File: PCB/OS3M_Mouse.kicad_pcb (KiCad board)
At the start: 4 copper layers, 60.8 x 61.3 mm, 47 parts, among them J1 DBG_HDR, J2 USB_C_Receptacle_USB2.0, J3 EXP_HDR, SW1 SW_Push, U1 AP2112K-3.3, U2 LDC1614, U3 STM32F042F6P6, U4 LDC1612, U5 USBLC6-2SC6, X1 ASV-40.000MHz

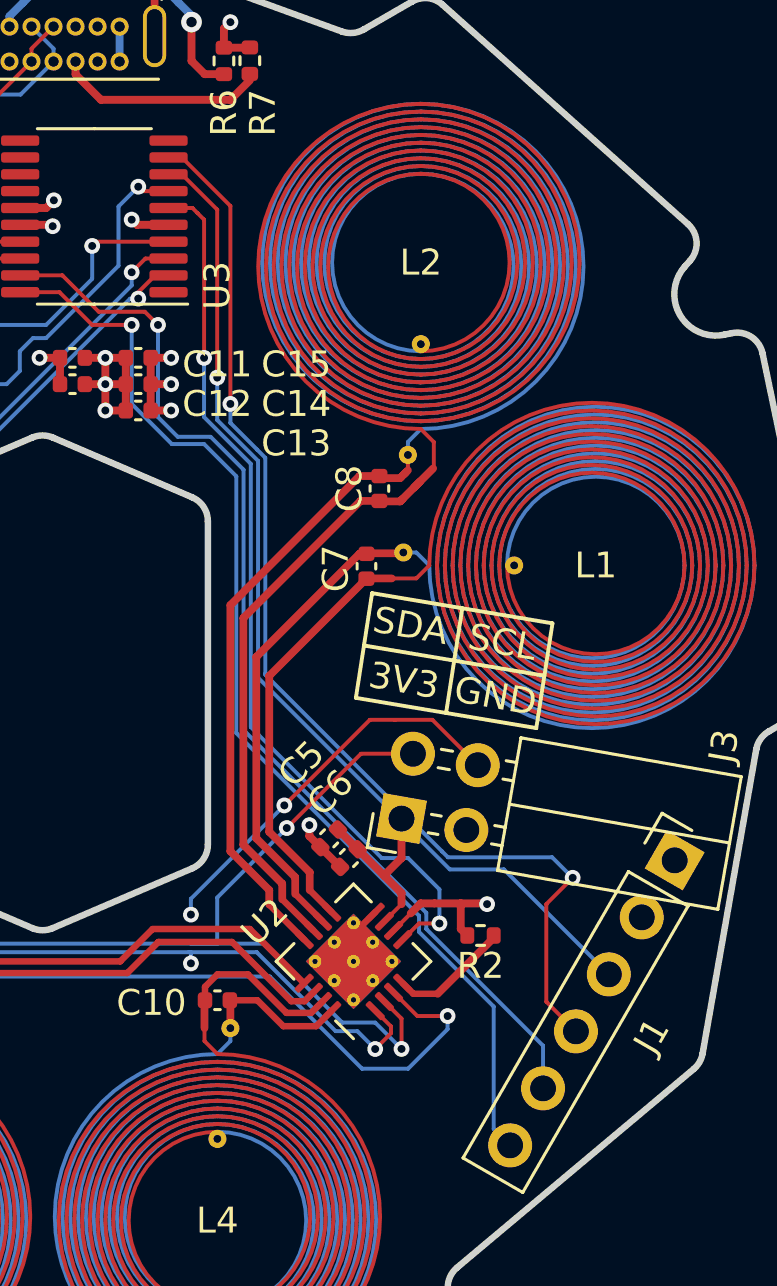
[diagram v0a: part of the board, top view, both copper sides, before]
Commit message: Fix shorted UART
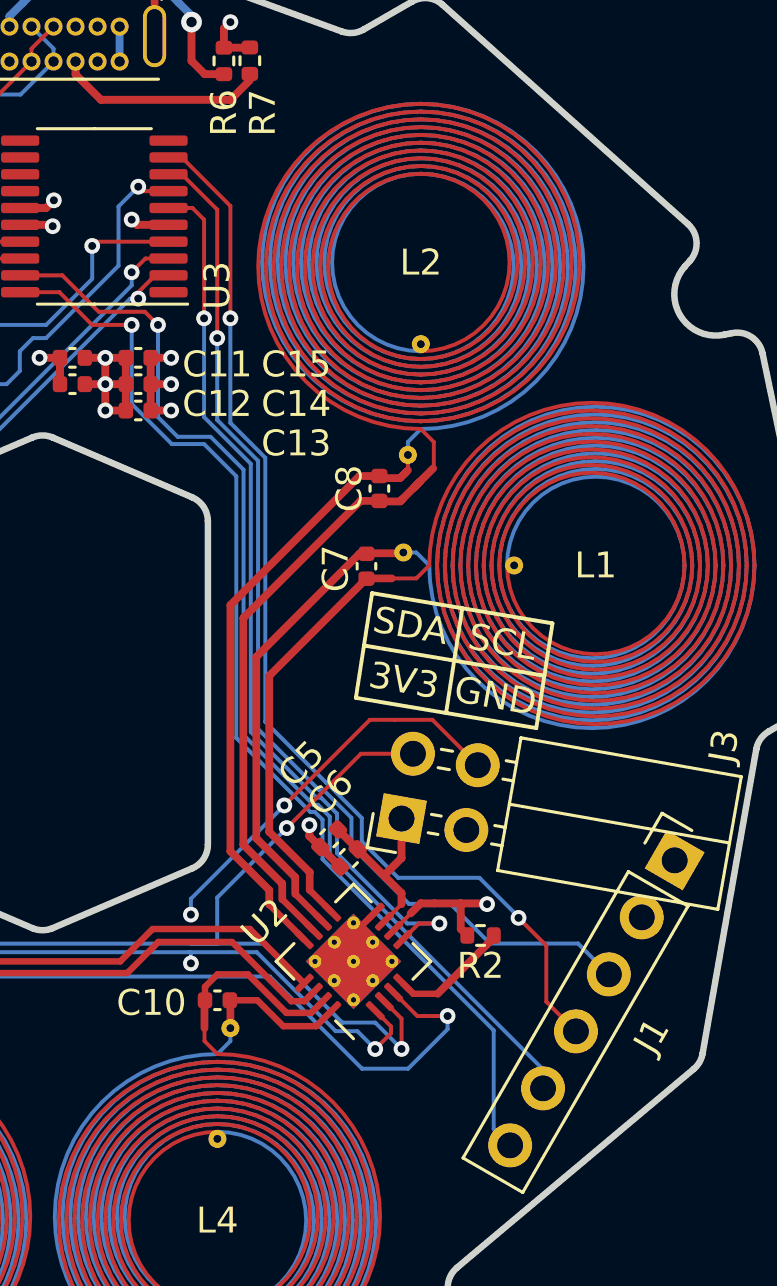
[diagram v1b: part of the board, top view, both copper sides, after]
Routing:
- net /UART2_TX: track 39.4 -> 41.2 mm
- net /UART2_RX: track 43.7 -> 42.4 mm

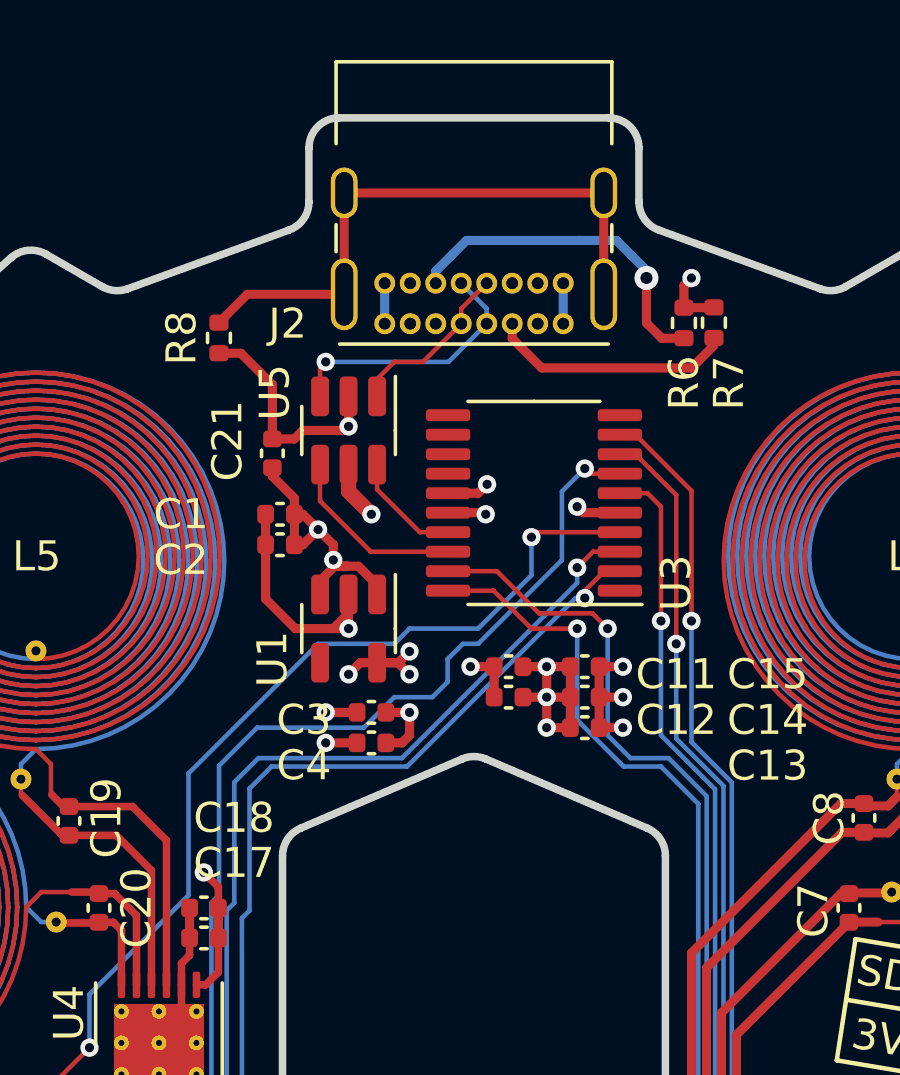
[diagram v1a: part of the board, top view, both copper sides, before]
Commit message: Update to Rev2, JLC manufacturable
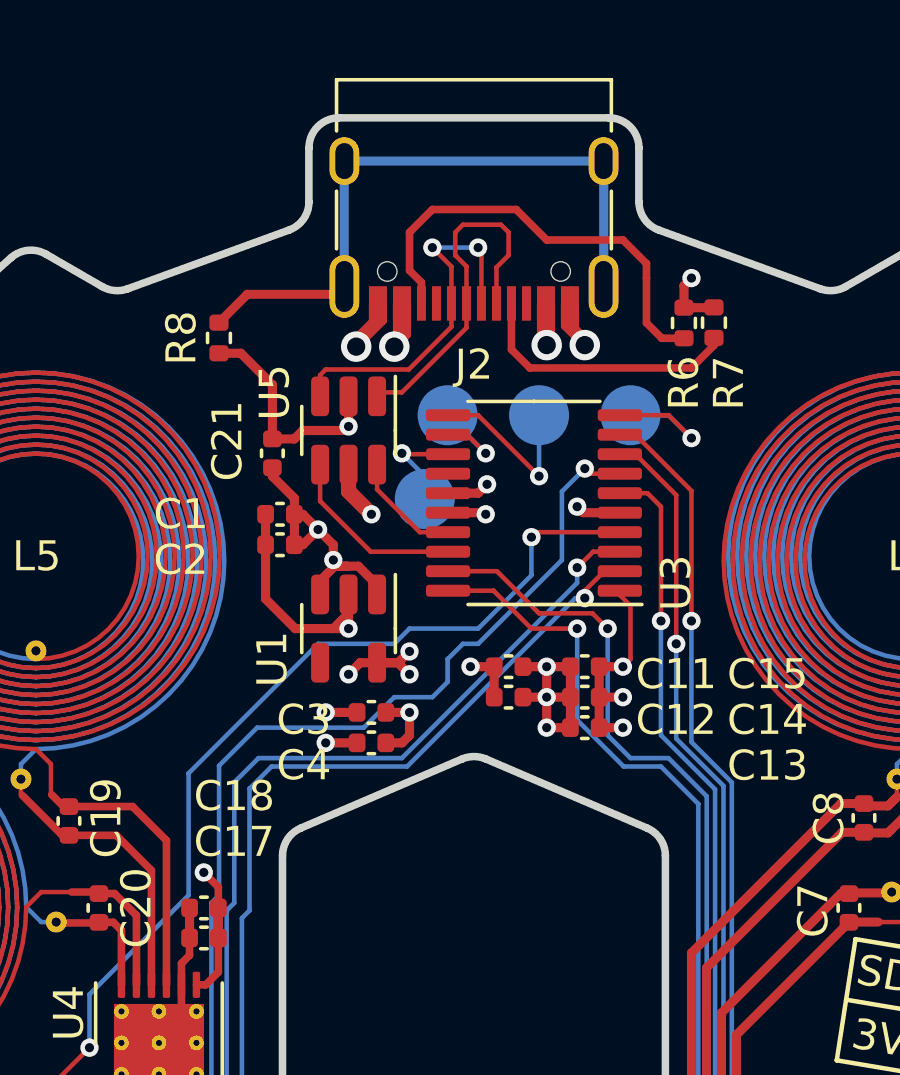
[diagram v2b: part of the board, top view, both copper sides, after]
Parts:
- added TP1: TestPoint, TestPoint:TestPoint_Pad_D2.0mm, B.Cu at (147.8, 74.7)
- added TP2: TestPoint, TestPoint:TestPoint_Pad_D2.0mm, B.Cu at (144.8, 74.7)
- added TP3: TestPoint, TestPoint:TestPoint_Pad_D2.0mm, B.Cu at (141.7, 74.7)
- added TP4: TestPoint, TestPoint:TestPoint_Pad_D2.0mm, B.Cu at (141.0, 77.5)
- J2: footprint Connector_USB:USB_C_Receptacle_GCT_USB4085 -> Connector_USB:USB_C_Receptacle_XKB_U262-16XN-4BVC11
- X1: value ASV-40.000MHz -> XTAL_40MHz
- moved J2 5.27 mm to (142.6, 67.3)
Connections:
- U3 pad 1: unconnected-(U3-Pad1) -> GND
- U3 pad 10: unconnected-(U3-Pad10) -> Net-(U3-Pad10)
- U3 pad 11: unconnected-(U3-Pad11) -> Net-(U3-Pad11)
- U3 pad 12: unconnected-(U3-Pad12) -> Net-(U3-Pad12)
- U3 pad 13: unconnected-(U3-Pad13) -> Net-(U3-Pad13)
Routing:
- net GND: track 65.8 -> 72.6 mm, vias 13 -> 15
- net VBUS: track 11.8 -> 17.7 mm, vias 3 -> 5
- net Net-(U3-Pad11): track 0.00 -> 5.91 mm, vias 0 -> 1
- net /USB_ESD_D-: track 6.00 -> 11.9 mm
- net Net-(U3-Pad10): track 0.00 -> 5.05 mm, vias 0 -> 1
- net /CC2: track 11.5 -> 14.9 mm, vias 1 -> 0
- net Net-(U3-Pad13): track 0.00 -> 3.39 mm, vias 0 -> 1
- net Net-(U3-Pad12): track 0.00 -> 3.31 mm, vias 0 -> 1
- net /USB_ESD_D+: track 8.96 -> 12.1 mm, vias 1 -> 2
- net Net-(J2-PadS1): track 20.0 -> 22.1 mm
- net /CC1: track 7.94 -> 9.10 mm
